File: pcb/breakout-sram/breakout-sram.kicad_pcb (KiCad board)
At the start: 4 copper layers, 62 x 62 mm, 6 parts, among them J1 FX18-120P-0.8SV20, J2 FX18-120S-0.8SV20, U1 IS61WV102416DBLL-10TLI

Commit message: [pcb] misc updates prior to ordder
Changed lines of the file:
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@@
 		(tags "capacitor")
 		(property "Reference" "C1"
-			(at 2.521 -0.014 270)
+			(at 2.521 -0.014 -90)
 			(layer "F.SilkS")
 			(effects
@@
 		)
 		(property "Value" "22uf"
-			(at 0 1.43 270)
+			(at 0 1.43 -90)
 			(layer "F.Fab")
 			(effects
@@
 		)
 		(fp_text user "${REFERENCE}"
-			(at 0 0 270)
+			(at 0 0 -90)
 			(layer "F.Fab")
 			(effects
@@
 		(sheetname "Root")
 		(sheetfile "breakout-sram.kicad_sch")
-		(attr smd)
+		(attr smd dnp)
 		(fp_circle
 			(center -26.701 -3.02)
@@
 		(sheetname "Root")
 		(sheetfile "breakout-sram.kicad_sch")
-		(attr smd)
+		(attr smd dnp)
 		(fp_circle
 			(center -26.701 -3.02)
@@
 		(tags "capacitor")
 		(property "Reference" "C2"
-			(at 0 -1.143 360)
+			(at 0 -1.143 0)
 			(layer "F.SilkS")
 			(effects
@@
 		)
 		(property "Value" "0.1uf"
-			(at 0 1.16 360)
+			(at 0 1.16 0)
 			(layer "F.Fab")
 			(effects
@@
 		)
 		(fp_text user "${REFERENCE}"
-			(at 0 0 360)
+			(at 0 0 0)
 			(layer "F.Fab")
 			(effects
@@
 		(tags "IS61WV102416DBLL-10TLI ")
 		(property "Reference" "U1"
-			(at 0.067 7.568552 0)
+			(at 0.027 7.678552 0)
 			(unlocked yes)
 			(layer "F.SilkS")
@@
 			)
 		)
-		(property "Footprint" "IS61WV102416DBLLIS61WV102416DBLL:IS61WV102416DBLL-10TLI_ISI"
+		(property "Footprint" "IS61WV102416DBLL-10TLI_ISI"
 			(at 0 0 0)
 			(unlocked yes)
@@
 			)
 		)
+		(property "LCSC Part #" " C1348726"
+			(at 0 0 0)
+			(unlocked yes)
+			(layer "F.Fab")
+			(hide yes)
+			(effects
+				(font
+					(size 1 1)
+					(thickness 0.15)
+				)
+			)
+		)
 		(property ki_fp_filters "IS61WV102416DBLL-10TLI_ISI IS61WV102416DBLL-10TLI_ISI-M IS61WV102416DBLL-10TLI_ISI-L")
 		(sheetname "Root")
@@
 		(fp_text user "*"
 			(at -8.9154 -6.0198 0)
+			(unlocked yes)
 			(layer "F.Fab")
 			(effects

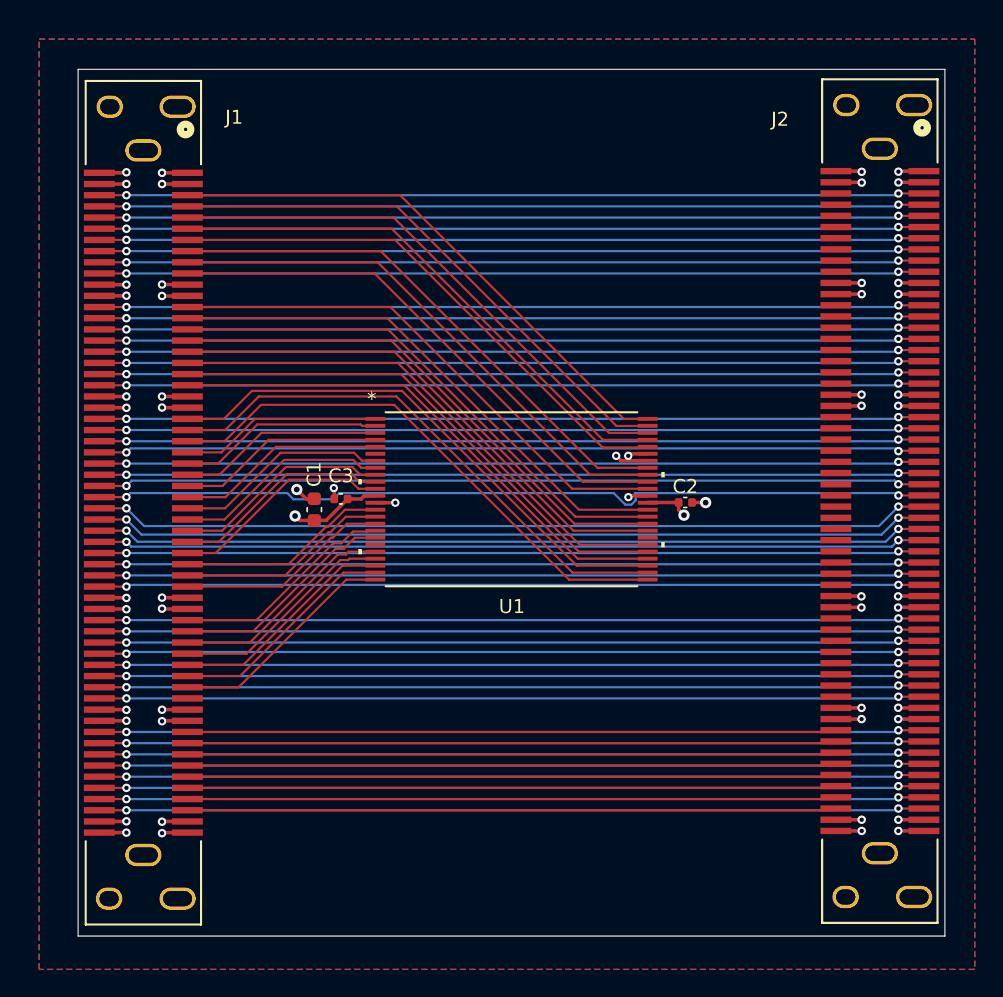
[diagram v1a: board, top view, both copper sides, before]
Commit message: [sram] update with correct nets labels
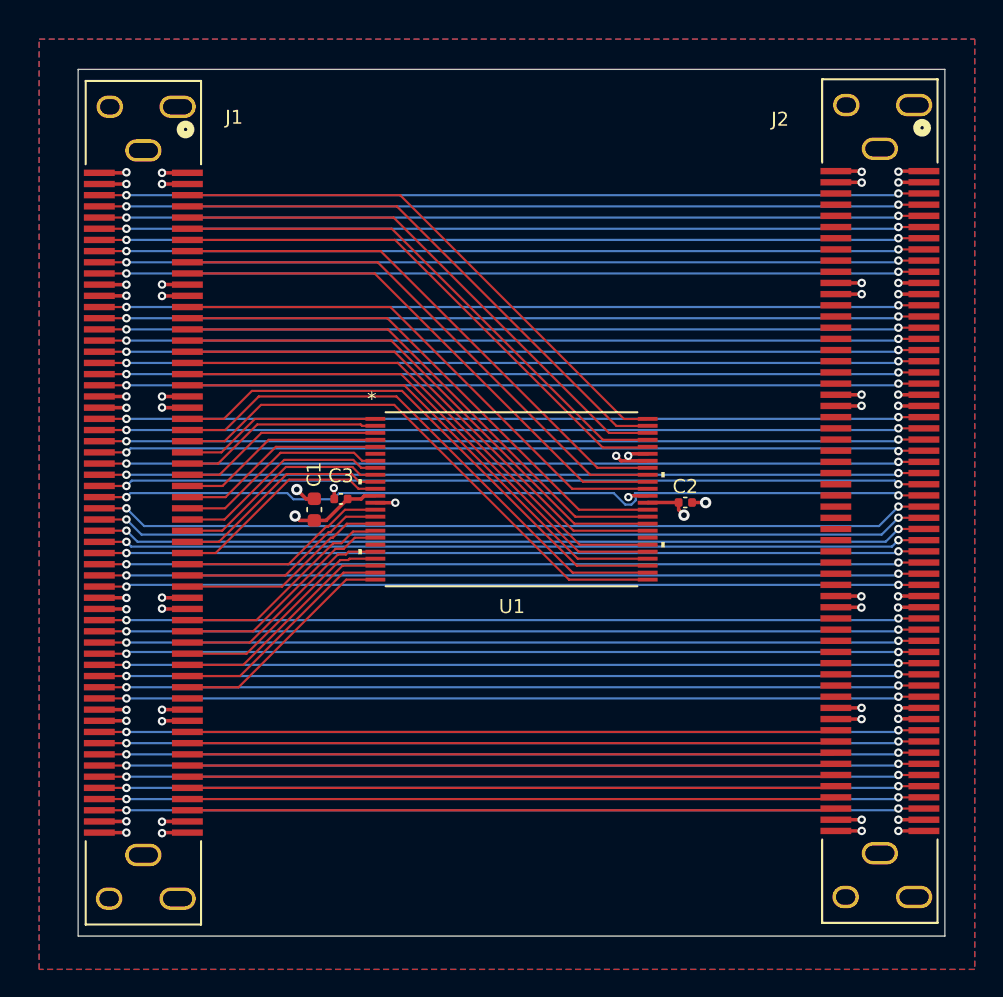
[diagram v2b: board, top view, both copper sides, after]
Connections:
- J1 pad 101: /JI_01 -> /JI_08
- J1 pad 102: /JI_02 -> /JI_04
- J1 pad 103: /JI_03 -> /JI_07
- J1 pad 104: /JI_04 -> /JI_03
- J1 pad 105: /JI_05 -> /JI_06
- J1 pad 106: /JI_06 -> /JI_02
- J1 pad 107: /JI_07 -> /JI_05
- J1 pad 108: /JI_08 -> /JI_01
- J1 pad 112: /LK_02 -> /LK_05
- J1 pad 113: /LK_03 -> /LK_02
- J1 pad 114: /LK_04 -> /LK_06
- J1 pad 115: /LK_05 -> /LK_03
- J1 pad 116: /LK_06 -> /LK_07
- J1 pad 117: /LK_07 -> /LK_04
- J1 pad 14: /CD_02 -> /CD_05
- J1 pad 15: /CD_03 -> /CD_02
- J1 pad 16: /CD_04 -> /CD_06
- J1 pad 17: /CD_05 -> /CD_03
- J1 pad 18: /CD_06 -> /CD_07
- J1 pad 19: /CD_07 -> /CD_04
- J1 pad 24: /EF_02 -> /EF_05
- J1 pad 25: /EF_03 -> /EF_02
- J1 pad 26: /EF_04 -> /EF_06
- J1 pad 27: /EF_05 -> /EF_03
- J1 pad 28: /EF_06 -> /EF_07
- J1 pad 29: /EF_07 -> /EF_04
- J1 pad 32: /GH_02 -> /GH_05
- J1 pad 33: /GH_03 -> /GH_02
- J1 pad 34: /GH_04 -> /GH_06
- J1 pad 35: /GH_05 -> /GH_03
- J1 pad 36: /GH_06 -> /GH_07
- J1 pad 37: /GH_07 -> /GH_04
- J1 pad 4: /AB_02 -> /AB_05
- J1 pad 42: /IJ_02 -> /IJ_05
- J1 pad 43: /IJ_03 -> /IJ_02
- J1 pad 44: /IJ_04 -> /IJ_06
- J1 pad 45: /IJ_05 -> /IJ_03
- J1 pad 46: /IJ_06 -> /IJ_07
- J1 pad 47: /IJ_07 -> /IJ_04
- J1 pad 5: /AB_03 -> /AB_02
- J1 pad 52: /KL_02 -> /KL_05
- J1 pad 53: /KL_03 -> /KL_02
- J1 pad 54: /KL_04 -> /KL_06
- J1 pad 55: /KL_05 -> /KL_03
- J1 pad 56: /KL_06 -> /KL_07
- J1 pad 57: /KL_07 -> /KL_04
- J1 pad 6: /AB_04 -> /AB_06
- J1 pad 64: /BA_02 -> /BA_05
- J1 pad 65: /BA_03 -> /BA_02
- J1 pad 66: /BA_04 -> /BA_06
- J1 pad 67: /BA_05 -> /BA_03
- J1 pad 68: /BA_06 -> /BA_07
- J1 pad 69: /BA_07 -> /BA_04
- J1 pad 7: /AB_05 -> /AB_03
- J1 pad 74: /DC_02 -> /DC_05
- J1 pad 75: /DC_03 -> /DC_02
- J1 pad 76: /DC_04 -> /DC_06
- J1 pad 77: /DC_05 -> /DC_03
- J1 pad 78: /DC_06 -> /DC_07
- J1 pad 79: /DC_07 -> /DC_04
- J1 pad 8: /AB_06 -> /AB_07
- J1 pad 83: /FE_01 -> /FE_08
- J1 pad 84: /FE_02 -> /FE_04
- J1 pad 85: /FE_03 -> /FE_07
- J1 pad 86: /FE_04 -> /FE_03
- J1 pad 87: /FE_05 -> /FE_06
- J1 pad 88: /FE_06 -> /FE_02
- J1 pad 89: /FE_07 -> /FE_05
- J1 pad 9: /AB_07 -> /AB_04
- J1 pad 90: /FE_08 -> /FE_01
- J1 pad 92: /HG_02 -> /HG_05
- J1 pad 93: /HG_03 -> /HG_02
- J1 pad 94: /HG_04 -> /HG_06
- J1 pad 95: /HG_05 -> /HG_03
- J1 pad 96: /HG_06 -> /HG_07
- J1 pad 97: /HG_07 -> /HG_04
- J2 pad 112: /KL_02 -> /KL_05
- J2 pad 113: /KL_03 -> /KL_02
- J2 pad 114: /KL_04 -> /KL_06
- J2 pad 115: /KL_05 -> /KL_03
- J2 pad 116: /KL_06 -> /KL_07
- J2 pad 117: /KL_07 -> /KL_04
- J2 pad 14: /DC_02 -> /DC_05
- J2 pad 15: /DC_03 -> /DC_02
- J2 pad 16: /DC_04 -> /DC_06
- J2 pad 17: /DC_05 -> /DC_03
- J2 pad 18: /DC_06 -> /DC_07
- J2 pad 19: /DC_07 -> /DC_04
- J2 pad 23: /FE_01 -> /FE_08
- J2 pad 24: /FE_02 -> /FE_04
- J2 pad 25: /FE_03 -> /FE_07
- J2 pad 26: /FE_04 -> /FE_03
- J2 pad 27: /FE_05 -> /FE_06
- J2 pad 28: /FE_06 -> /FE_02
- J2 pad 29: /FE_07 -> /FE_05
- J2 pad 30: /FE_08 -> /FE_01
- J2 pad 32: /HG_02 -> /HG_05
- J2 pad 33: /HG_03 -> /HG_02
- J2 pad 34: /HG_04 -> /HG_06
- J2 pad 35: /HG_05 -> /HG_03
- J2 pad 36: /HG_06 -> /HG_07
- J2 pad 37: /HG_07 -> /HG_04
- J2 pad 4: /BA_02 -> /BA_05
- J2 pad 41: /JI_01 -> /JI_08
- J2 pad 42: /JI_02 -> /JI_04
- J2 pad 43: /JI_03 -> /JI_07
- J2 pad 44: /JI_04 -> /JI_03
- J2 pad 45: /JI_05 -> /JI_06
- J2 pad 46: /JI_06 -> /JI_02
- J2 pad 47: /JI_07 -> /JI_05
- J2 pad 48: /JI_08 -> /JI_01
- J2 pad 5: /BA_03 -> /BA_02
- J2 pad 52: /LK_02 -> /LK_05
- J2 pad 53: /LK_03 -> /LK_02
- J2 pad 54: /LK_04 -> /LK_06
- J2 pad 55: /LK_05 -> /LK_03
- J2 pad 56: /LK_06 -> /LK_07
- J2 pad 57: /LK_07 -> /LK_04
- J2 pad 6: /BA_04 -> /BA_06
- J2 pad 7: /BA_05 -> /BA_03
- J2 pad 8: /BA_06 -> /BA_07
- J2 pad 9: /BA_07 -> /BA_04
- U1 pad 1: /EF_04 -> /EF_06
- U1 pad 10: /GH_04 -> /GH_06
- U1 pad 11: /GH_05 -> /GH_03
- U1 pad 14: /GH_06 -> /GH_07
- U1 pad 15: /GH_07 -> /GH_04
- U1 pad 18: /IJ_02 -> /IJ_05
- U1 pad 2: /EF_05 -> /EF_03
- U1 pad 20: /IJ_03 -> /IJ_02
- U1 pad 21: /IJ_04 -> /IJ_06
- U1 pad 22: /IJ_05 -> /IJ_03
- U1 pad 23: /IJ_06 -> /IJ_07
- U1 pad 24: /IJ_07 -> /IJ_04
- U1 pad 25: /EF_03 -> /EF_02
- U1 pad 26: /EF_02 -> /EF_05
- U1 pad 29: /CD_07 -> /CD_04
- U1 pad 3: /EF_06 -> /EF_07
- U1 pad 30: /CD_06 -> /CD_07
- U1 pad 32: /CD_05 -> /CD_03
- U1 pad 33: /CD_04 -> /CD_06
- U1 pad 34: /CD_03 -> /CD_02
- U1 pad 35: /CD_02 -> /CD_05
- U1 pad 4: /EF_07 -> /EF_04
- U1 pad 40: /AB_07 -> /AB_04
- U1 pad 41: /AB_06 -> /AB_07
- U1 pad 44: /AB_05 -> /AB_03
- U1 pad 45: /AB_04 -> /AB_06
- U1 pad 46: /AB_03 -> /AB_02
- U1 pad 47: /AB_02 -> /AB_05
- U1 pad 8: /GH_02 -> /GH_05
- U1 pad 9: /GH_03 -> /GH_02
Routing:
- net /EF_03: track 39.2 -> 14.6 mm
- net /EF_05: track 14.6 -> 39.1 mm
- net /FE_08: track 60.6 -> 59.0 mm
- net /FE_01: track 59.0 -> 60.6 mm
- net /HG_05: track 59.0 -> 59.9 mm
- net /HG_03: track 59.7 -> 59.0 mm
- net /GH_06: track 15.1 -> 15.7 mm

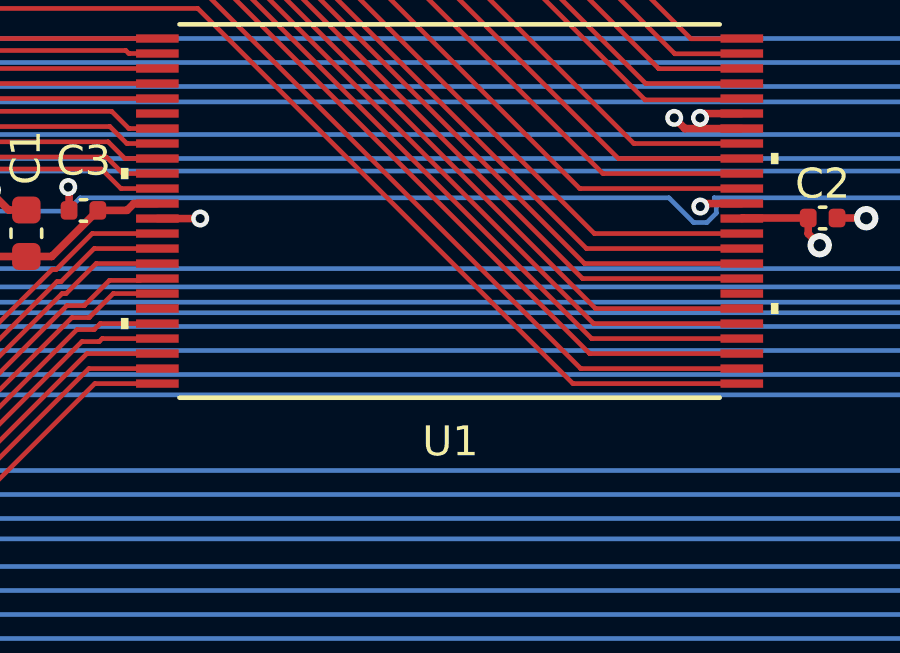
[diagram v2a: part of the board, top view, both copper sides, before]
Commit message: [pcb][sram] switch to single letter labels
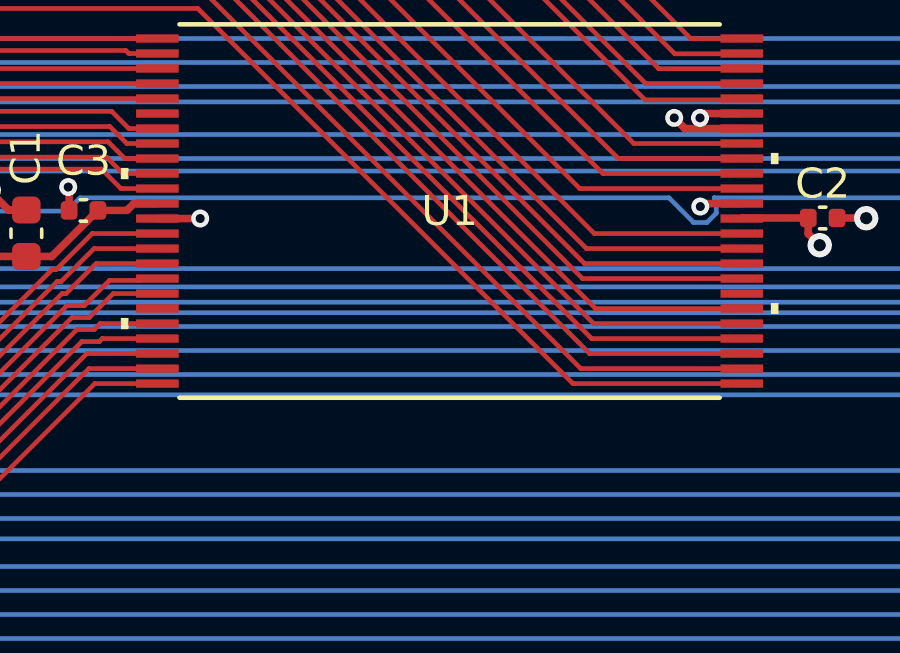
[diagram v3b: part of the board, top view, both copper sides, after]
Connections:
- net /AB_01 renamed /A_01
- net /AB_02 renamed /A_02
- net /AB_03 renamed /A_03
- net /AB_04 renamed /A_04
- net /AB_05 renamed /A_05
- net /AB_06 renamed /A_06
- net /AB_07 renamed /A_07
- net /AB_08 renamed /A_08
- net /BA_01 renamed /E_01
- net /BA_02 renamed /E_02
- net /BA_03 renamed /E_03
- net /BA_04 renamed /E_04
- net /BA_05 renamed /E_05
- net /BA_06 renamed /E_06
- net /BA_07 renamed /E_07
- net /BA_08 renamed /E_08
- net /CD_01 renamed /B_01
- net /CD_02 renamed /B_02
- net /CD_03 renamed /B_03
- net /CD_04 renamed /B_04
- net /CD_05 renamed /B_05
- net /CD_06 renamed /B_06
- net /CD_07 renamed /B_07
- net /CD_08 renamed /B_08
- net /DC_01 renamed /F_01
- net /DC_02 renamed /F_02
- net /DC_03 renamed /F_03
- net /DC_04 renamed /F_04
- net /DC_05 renamed /F_05
- net /DC_06 renamed /F_06
- net /DC_07 renamed /F_07
- net /DC_08 renamed /F_08
- net /EF_01 renamed /C_01
- net /EF_02 renamed /C_02
- net /EF_03 renamed /C_03
- net /EF_04 renamed /C_04
- net /EF_05 renamed /C_05
- net /EF_06 renamed /C_06
- net /EF_07 renamed /C_07
- net /EF_08 renamed /C_08
- net /FE_01 renamed /L_01
- net /FE_02 renamed /L_02
- net /FE_03 renamed /L_03
- net /FE_04 renamed /L_04
- net /FE_05 renamed /L_05
- net /FE_06 renamed /L_06
- net /FE_07 renamed /L_07
- net /FE_08 renamed /L_08
- net /GH_01 renamed /D_01
- net /GH_02 renamed /D_02
- net /GH_03 renamed /D_03
- net /GH_04 renamed /D_04
- net /GH_05 renamed /D_05
- net /GH_06 renamed /D_06
- net /GH_07 renamed /D_07
- net /GH_08 renamed /D_08
- net /HG_01 renamed /I_01
- net /HG_02 renamed /I_02
- net /HG_03 renamed /I_03
- net /HG_04 renamed /I_04
- net /HG_05 renamed /I_05
- net /HG_06 renamed /I_06
- net /HG_07 renamed /I_07
- net /HG_08 renamed /I_08
- net /IJ_01 renamed /G_01
- net /IJ_02 renamed /G_02
- net /IJ_03 renamed /G_03
- net /IJ_04 renamed /G_04
- net /IJ_05 renamed /G_05
- net /IJ_06 renamed /G_06
- net /IJ_07 renamed /G_07
- net /IJ_08 renamed /G_08
- net /JI_01 renamed /K_01
- net /JI_02 renamed /K_02
- net /JI_03 renamed /K_03
- net /JI_04 renamed /K_04
- net /JI_05 renamed /K_05
- net /JI_06 renamed /K_06
- net /JI_07 renamed /K_07
- net /JI_08 renamed /K_08
- net /KL_01 renamed /H_01
- net /KL_02 renamed /H_02
- net /KL_03 renamed /H_03
- net /KL_04 renamed /H_04
- net /KL_05 renamed /H_05
- net /KL_06 renamed /H_06
- net /KL_07 renamed /H_07
- net /KL_08 renamed /H_08
- net /LK_01 renamed /J_01
- net /LK_02 renamed /J_02
- net /LK_03 renamed /J_03
- net /LK_04 renamed /J_04
- net /LK_05 renamed /J_05
- net /LK_06 renamed /J_06
- net /LK_07 renamed /J_07
- net /LK_08 renamed /J_08

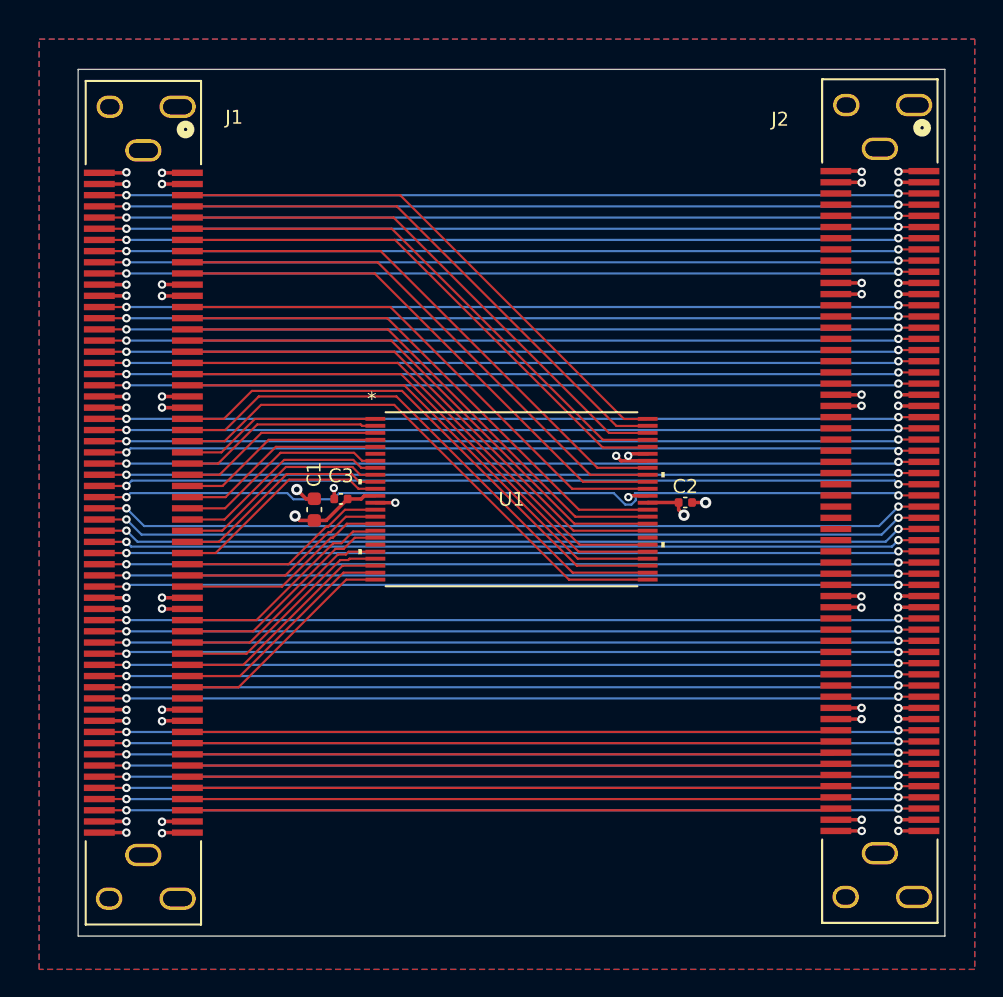
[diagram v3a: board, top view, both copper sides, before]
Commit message: [pcb][sram] tidy up routing
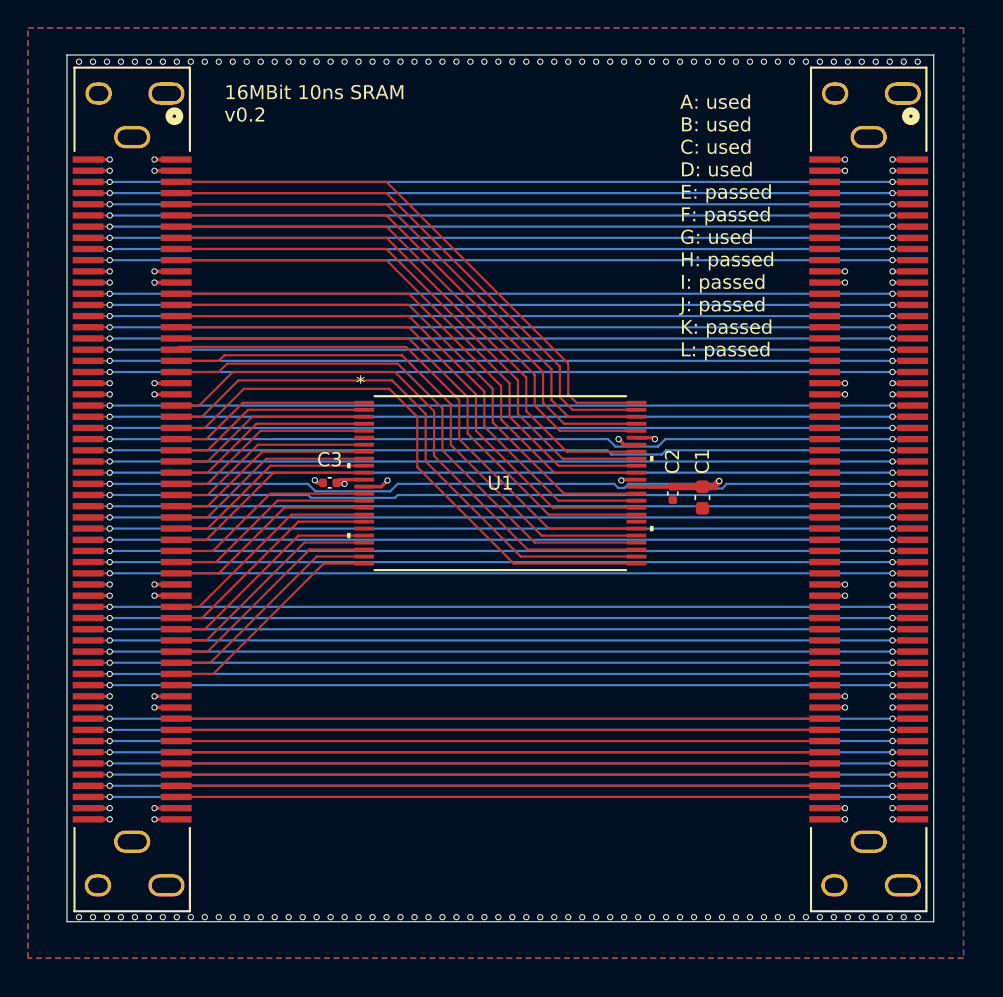
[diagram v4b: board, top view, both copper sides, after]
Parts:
- added REF**: OSHW-Logo2_14.6x12mm_SilkScreen, Symbol:OSHW-Logo2_14.6x12mm_SilkScreen, B.Cu at (95.0, 93.0)
- moved C1 27.8 mm to (96.6, 73.2), turned to -90 degrees
- moved C3 1.40 mm to (69.9, 72.1)
- moved U1 1.40 mm to (82.1, 72.2)
- moved J1 1.24 mm to (55.8, 72.6)
- moved J2 1.15 mm to (108.5, 72.6)
- moved C2 1.11 mm to (94.5, 72.9), turned to -90 degrees
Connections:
- J1 pad 48: /G_08 -> unconnected-(J1-Pad48)
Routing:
- net GND: track 54.7 -> 42.5 mm, vias 31 -> 151
- net +3V3: track 54.6 -> 46.1 mm
- net /C_02: track 39.2 -> 41.4 mm
- net /B_08: track 38.1 -> 40.2 mm
- net /C_01: track 38.9 -> 41.1 mm
- net /C_05: track 39.1 -> 41.2 mm
- net /B_04: track 38.2 -> 40.1 mm
- net /B_07: track 38.3 -> 40.0 mm
- net /B_03: track 38.2 -> 39.7 mm
- net /B_06: track 38.4 -> 39.8 mm
- net /B_02: track 38.5 -> 39.9 mm
- net /A_04: track 39.2 -> 40.5 mm
- net /A_08: track 39.1 -> 40.4 mm
- net /A_07: track 39.3 -> 40.7 mm
- net /B_05: track 38.6 -> 39.9 mm
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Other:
- board text added: "16MBit 10ns SRAM"
- board text added: "A: used B: used C: used D: used E: passed F: passed G: used H: passed I: passed J: passed K: passed L: passed"
- board text added: "git@github.com:pbozeman/vanilla-ice40.git"
- board text added: "v0.2"
- board text added: "www.pbozeman.dev"
